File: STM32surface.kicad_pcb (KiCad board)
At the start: 2 copper layers, 26 x 66 mm, 25 parts, among them J3 USB_B, J4 Conn_01x04, J5 Conn_01x20, J6 Conn_02x03_Odd_Even, J7 Conn_01x02, J9 Conn_01x20, U1 AMS1117-3V3, U2 STM32F103C8T6, Y1 8 MHz, Y2 Crystal

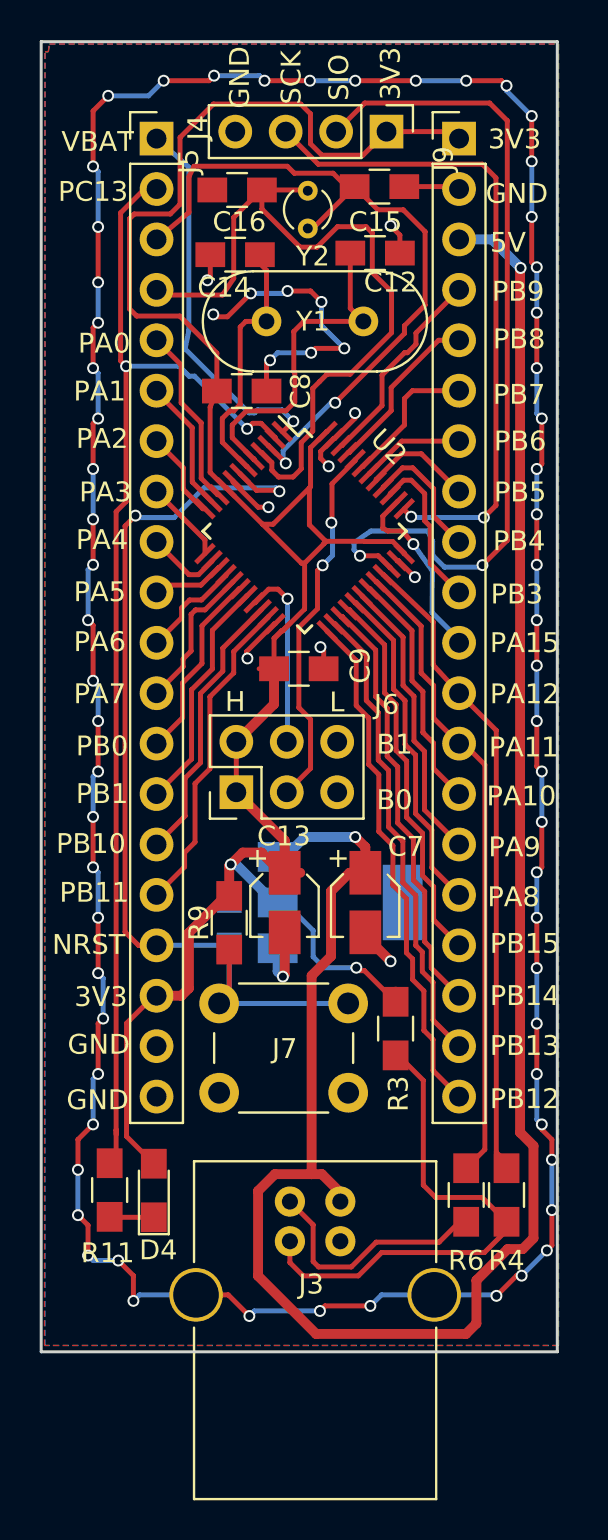
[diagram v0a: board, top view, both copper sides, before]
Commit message: Changed all to JLCPCB parts
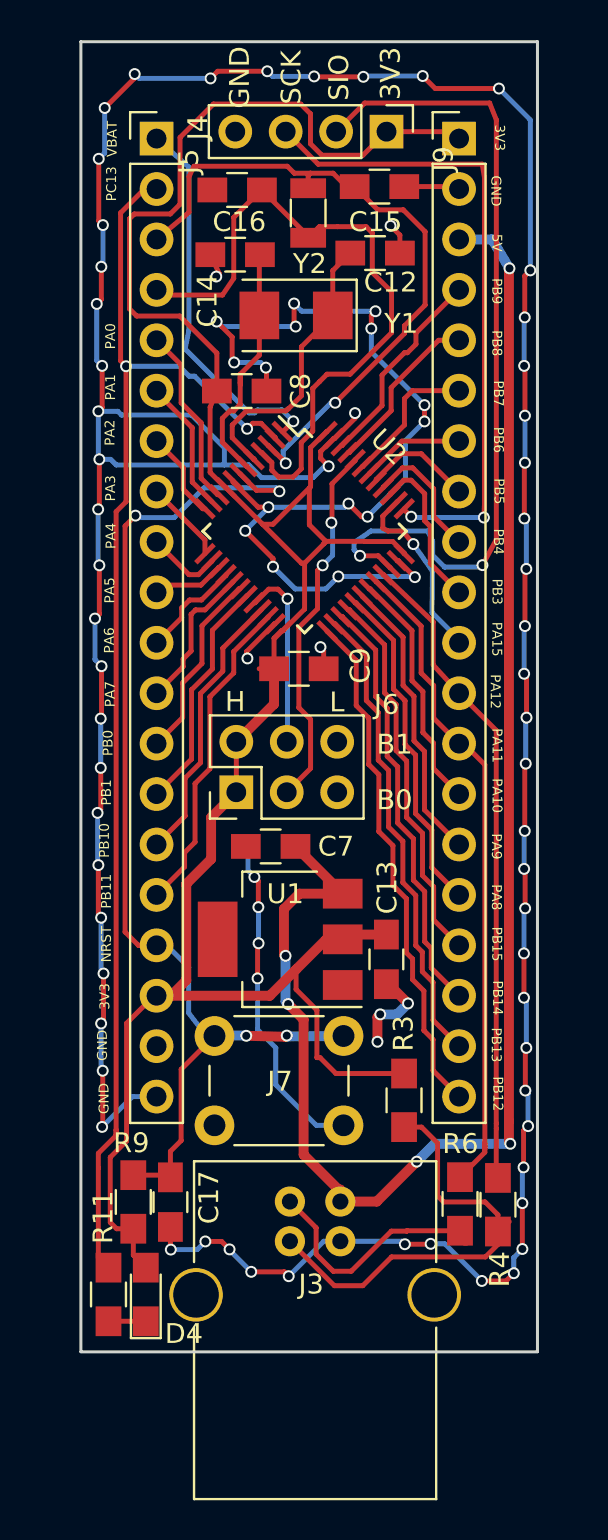
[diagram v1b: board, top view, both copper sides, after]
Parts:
- C13, C7: footprint Capacitors_SMD:CP_Elec_3x5.3 -> Capacitors_SMD:C_0805_HandSoldering
- C17, U1: moved to F.Cu
- Y1: footprint Crystals:Crystal_HC49-U_Vertical -> Crystals:Crystal_SMD_5032-2pin_5.0x3.2mm
- Y2: footprint Crystals:Crystal_Round_d2.0mm_Vertical -> Crystals:Crystal_SMD_3215-2pin_3.2x1.5mm
- moved R9 14.9 mm to (59.9, 87.7), turned to 90 degrees
- moved C17 14.4 mm to (61.8, 87.7), turned to 270 degrees
- moved C13 5.87 mm to (72.7, 75.5), turned to 90 degrees
- moved C7 5.55 mm to (66.9, 69.8), turned to 0 degrees
- moved R11 5.26 mm to (58.7, 92.4)
- moved D4 5.25 mm to (60.6, 92.4)
- moved R3 3.64 mm to (73.6, 82.6)
- moved U1 3.54 mm to (67.3, 74.5), turned to 180 degrees
- moved Y1 3.40 mm to (68.1, 43.1)
- moved J7 1.66 mm to (64.0, 79.4)
- moved Y2 1.12 mm to (68.7, 37.9)
- moved R4 0.65 mm to (78.3, 87.9)
- moved R6 0.55 mm to (76.4, 87.8)
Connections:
- C13 pad 1: 3V3B -> GNDB
- C13 pad 2: GNDB -> 3V3B
- C7 pad 1: 5VB -> GNDB
- C7 pad 2: GNDB -> 5VB
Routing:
- net GNDB: track 205.2 -> 262.4 mm, vias 80 -> 88
- net 5VB: track 103.9 -> 80.8 mm, vias 2 -> 5
- net 3V3B: track 116.6 -> 127.1 mm, vias 2 -> 0
- net NRST: track 51.1 -> 58.4 mm, vias 2 -> 4
- net PC13: track 60.1 -> 65.8 mm
- net OSC32OUT: track 37.4 -> 34.1 mm
- net Net-(J3-Pad3): track 25.8 -> 23.2 mm
- net OSC32IN: track 36.8 -> 34.4 mm
- net OSCIN: track 16.9 -> 14.6 mm
- net PA11: track 32.7 -> 33.5 mm
- net PA13: track 43.0 -> 42.4 mm
- net PA14: track 33.1 -> 32.6 mm
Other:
- board size 26 x 66 mm -> 23 x 66 mm
